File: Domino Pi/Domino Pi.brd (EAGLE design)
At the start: 71.1 x 33 mm, 77 parts, among them J1 MH28-1, J2 MH28-1, M1 DOMINO, SW1 IT-1210, U1 MP65151DJ, U2 MP2162GQH, U3 CP2104-F03-GM, U4 74LVC1G125DCK

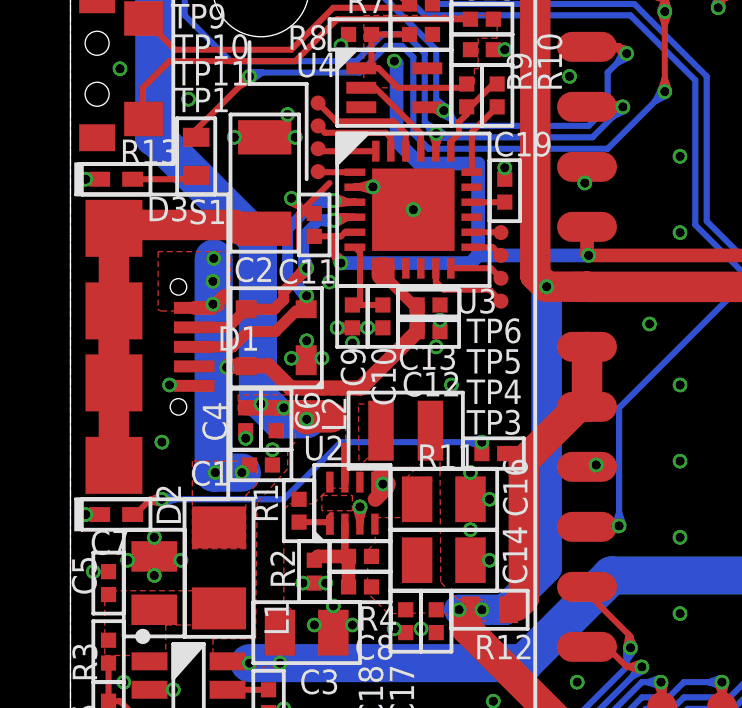
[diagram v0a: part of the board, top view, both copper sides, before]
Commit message: Domino Pi Rev.D: removed some leftover traces within poured areas
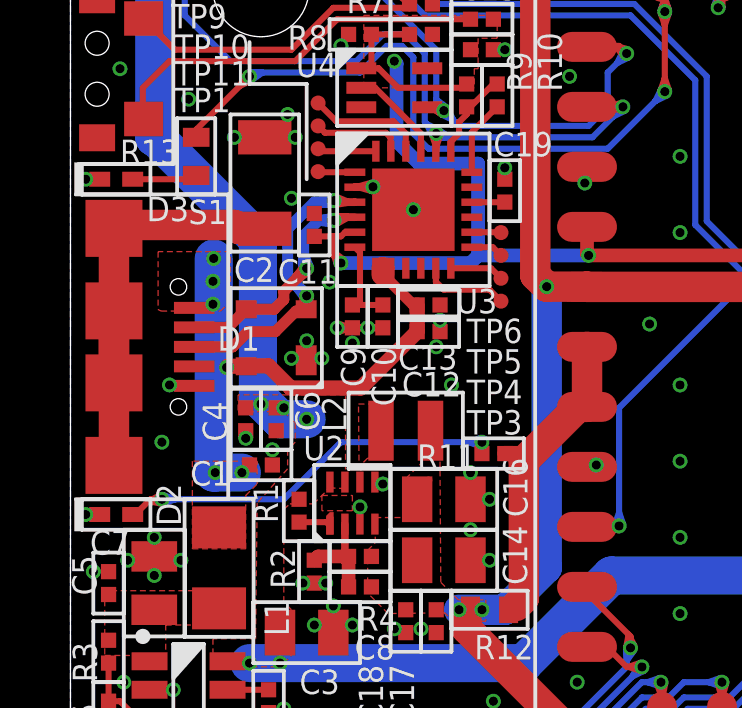
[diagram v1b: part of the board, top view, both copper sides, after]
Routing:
- net GND: track 16.3 -> 8.25 mm
- net +5V: track 86.7 -> 81.6 mm
- net VBUS: track 20.3 -> 19.2 mm
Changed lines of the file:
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@@
 <layers>
 <layer number="1" name="Top" color="4" fill="1" visible="yes" active="yes"/>
-<layer number="16" name="Bottom" color="1" fill="1" visible="no" active="yes"/>
+<layer number="16" name="Bottom" color="1" fill="1" visible="yes" active="yes"/>
 <layer number="17" name="Pads" color="2" fill="1" visible="yes" active="yes"/>
 <layer number="18" name="Vias" color="2" fill="1" visible="yes" active="yes"/>
@@
 <contactref element="J1" pad="18"/>
 <wire x1="9.340003125" y1="17.145" x2="8.9154" y2="17.145" width="0.2032" layer="1"/>
-<wire x1="8.128" y1="20.955" x2="7.874" y2="20.955" width="0.2032" layer="1"/>
-<wire x1="7.874" y1="20.955" x2="7.8105" y2="21.0185" width="0.2032" layer="1"/>
-<wire x1="7.8105" y1="21.0185" x2="7.6842" y2="21.1448" width="0.2032" layer="1"/>
-<wire x1="7.6842" y1="21.1448" x2="7.366" y2="21.463" width="0.2032" layer="1"/>
-<wire x1="7.62" y1="20.828" x2="7.8105" y2="21.0185" width="0.2032" layer="1"/>
 <wire x1="9.48" y1="21.832" x2="9.492" y2="21.844" width="0.254" layer="1"/>
 <wire x1="9.492" y1="21.844" x2="9.633796875" y2="21.844" width="0.254" layer="1"/>
@@
 <via x="8.636" y="18.669" extent="1-16" drill="0.3" diameter="0.0254"/>
 <via x="8.89" y="17.145" extent="1-16" drill="0.3" diameter="0.0254"/>
-<wire x1="9.633796875" y1="21.844" x2="10.0838" y2="21.844" width="0.254" layer="1"/>
-<wire x1="9.652" y1="11.176" x2="9.779" y2="11.176" width="0.254" layer="1"/>
-<wire x1="10.287" y1="12.192" x2="10.414" y2="12.192" width="0.508" layer="1"/>
-<wire x1="10.541" y1="11.938" x2="10.541" y2="11.811" width="0.508" layer="1"/>
-<wire x1="10.541" y1="11.811" x2="10.16" y2="11.43" width="0.508" layer="1"/>
-<wire x1="9.648" y1="10.603" x2="9.648" y2="10.726015625" width="0.254" layer="1"/>
-<wire x1="9.648" y1="10.726015625" x2="9.648" y2="11.172" width="0.254" layer="1"/>
-<wire x1="9.648" y1="11.172" x2="9.652" y2="11.176" width="0.254" layer="1"/>
-<wire x1="10.541" y1="11.938" x2="10.414" y2="11.938" width="0.6096" layer="1"/>
-<wire x1="10.414" y1="11.938" x2="10.414" y2="12.065" width="0.6096" layer="1"/>
 <via x="14.478" y="22.479" extent="1-16" drill="0.3" diameter="0.0254"/>
 <via x="12.319" y="17.399" extent="1-16" drill="0.3" diameter="0.0254"/>
@@
 <via x="8.128" y="7.239" extent="1-16" drill="0.3" diameter="0.0254"/>
 <via x="10.414" y="11.938" extent="1-16" drill="0.3" diameter="0.0254"/>
-<wire x1="10.287" y1="12.192" x2="10.287" y2="12.142" width="0.254" layer="1"/>
 <via x="0.508" y="10.922" extent="1-16" drill="0.3" diameter="0.0254"/>
 <via x="0.508" y="22.098" extent="1-16" drill="0.3" diameter="0.0254"/>
@@
 <contactref element="SW1" pad="SH$2"/>
 <contactref element="SW1" pad="SH$1"/>
-<wire x1="8.636" y1="21.971" x2="7.62" y2="20.955" width="0.2032" layer="1"/>
-<wire x1="7.62" y1="20.955" x2="7.62" y2="20.828" width="0.2032" layer="1"/>
-<wire x1="7.62" y1="20.828" x2="7.62" y2="19.685" width="0.2032" layer="1"/>
+<wire x1="9.633796875" y1="21.844" x2="10.0838" y2="21.844" width="0.254" layer="1"/>
 <wire x1="11.43" y1="21.082" x2="11.1118" y2="21.4002" width="0.254" layer="1"/>
 <wire x1="11.1118" y1="21.4002" x2="10.668" y2="21.844" width="0.254" layer="1"/>
@@
 <via x="3.048" y="13.335" extent="1-16" drill="0.3"/>
 <wire x1="10.533803125" y1="21.844" x2="10.668" y2="21.844" width="0.254" layer="1"/>
-<wire x1="9.648" y1="10.726015625" x2="9.7700125" y2="11.141325" width="0.254" layer="1"/>
-<wire x1="9.652" y1="11.176" x2="9.7700125" y2="11.141325" width="0.254" layer="1"/>
-<wire x1="9.648" y1="10.726015625" x2="9.5333875" y2="11.143428125" width="0.254" layer="1"/>
-<wire x1="9.652" y1="11.176" x2="9.5333875" y2="11.143428125" width="0.254" layer="1"/>
 <wire x1="11.1118" y1="21.4002" x2="11.3225625" y2="21.0221125" width="0.254" layer="1"/>
 <wire x1="11.43" y1="21.082" x2="11.3225625" y2="21.0221125" width="0.254" layer="1"/>
 <wire x1="11.1118" y1="21.4002" x2="11.489884375" y2="21.189434375" width="0.254" layer="1"/>
 <wire x1="11.43" y1="21.082" x2="11.489884375" y2="21.189434375" width="0.254" layer="1"/>
-<wire x1="7.6842" y1="21.1448" x2="7.49966875" y2="21.52745625" width="0.2032" layer="1"/>
-<wire x1="7.366" y1="21.463" x2="7.49966875" y2="21.52745625" width="0.2032" layer="1"/>
-<wire x1="7.6842" y1="21.1448" x2="7.301540625" y2="21.329328125" width="0.2032" layer="1"/>
-<wire x1="7.366" y1="21.463" x2="7.301540625" y2="21.329328125" width="0.2032" layer="1"/>
 <wire x1="9.633796875" y1="21.844" x2="10.050175" y2="21.72568125" width="0.254" layer="1"/>
 <wire x1="10.0838" y1="21.844" x2="10.050175" y2="21.72568125" width="0.254" layer="1"/>
@@
 <wire x1="10.414" y1="19.132" x2="10.68" y2="19.132" width="0.254" layer="1"/>
 <contactref element="S1" pad="1"/>
-<wire x1="4.125" y1="17.81" x2="4.729" y2="17.81" width="0.4572" layer="1"/>
-<wire x1="4.729" y1="17.81" x2="5.1308" y2="18.2118" width="0.4572" layer="1"/>
 <wire x1="11.557" y1="17.907" x2="11.43" y2="17.907" width="0.3683" layer="1"/>
 <wire x1="11.43" y1="17.907" x2="10.414" y2="18.923" width="0.3683" layer="1"/>
@@
 <contactref element="C6" pad="1"/>
 <contactref element="U2" pad="7"/>
-<wire x1="9.148" y1="12.003" x2="9.148" y2="13.204" width="0.254" layer="1"/>
-<wire x1="6.858" y1="14.478" x2="8.382" y2="14.478" width="0.508" layer="1"/>
-<wire x1="8.382" y1="14.478" x2="8.6995" y2="14.1605" width="0.508" layer="1"/>
-<wire x1="5.842" y1="14.478" x2="6.858" y2="14.478" width="0.508" layer="1"/>
 <contactref element="J1" pad="1"/>
 <via x="6.35" y="14.605" extent="1-16" drill="0.3" diameter="0.0254"/>
@@
 <wire x1="6.985" y1="14.097" x2="7.874" y2="14.097" width="1.27" layer="16"/>
 <via x="7.874" y="14.097" extent="1-16" drill="0.3"/>
-<wire x1="7.874" y1="14.097" x2="7.8105" y2="14.1605" width="1.016" layer="1"/>
-<wire x1="7.8105" y1="14.1605" x2="8.6995" y2="14.1605" width="1.016" layer="1"/>
 <via x="7.112" y="14.478" extent="1-16" drill="0.3" diameter="0.0254"/>
 <wire x1="62.23" y1="1.27" x2="54.61" y2="8.89" width="1.27" layer="16"/>
